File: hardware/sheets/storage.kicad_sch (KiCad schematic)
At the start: 32 parts, among them J1 Conn_02x20_Odd_Even, J2 Conn_02x25_Odd_Even, Q1 2N7002, U1 74HCT04, U10 74HCT573, U11 74HCT138, U2 74HCT08, U3 74HCT08, U4 74HCT32, U5 74HCT125, U6 74HCT138, U7 74HCT138, U8 74HCT245, U9 74HCT573

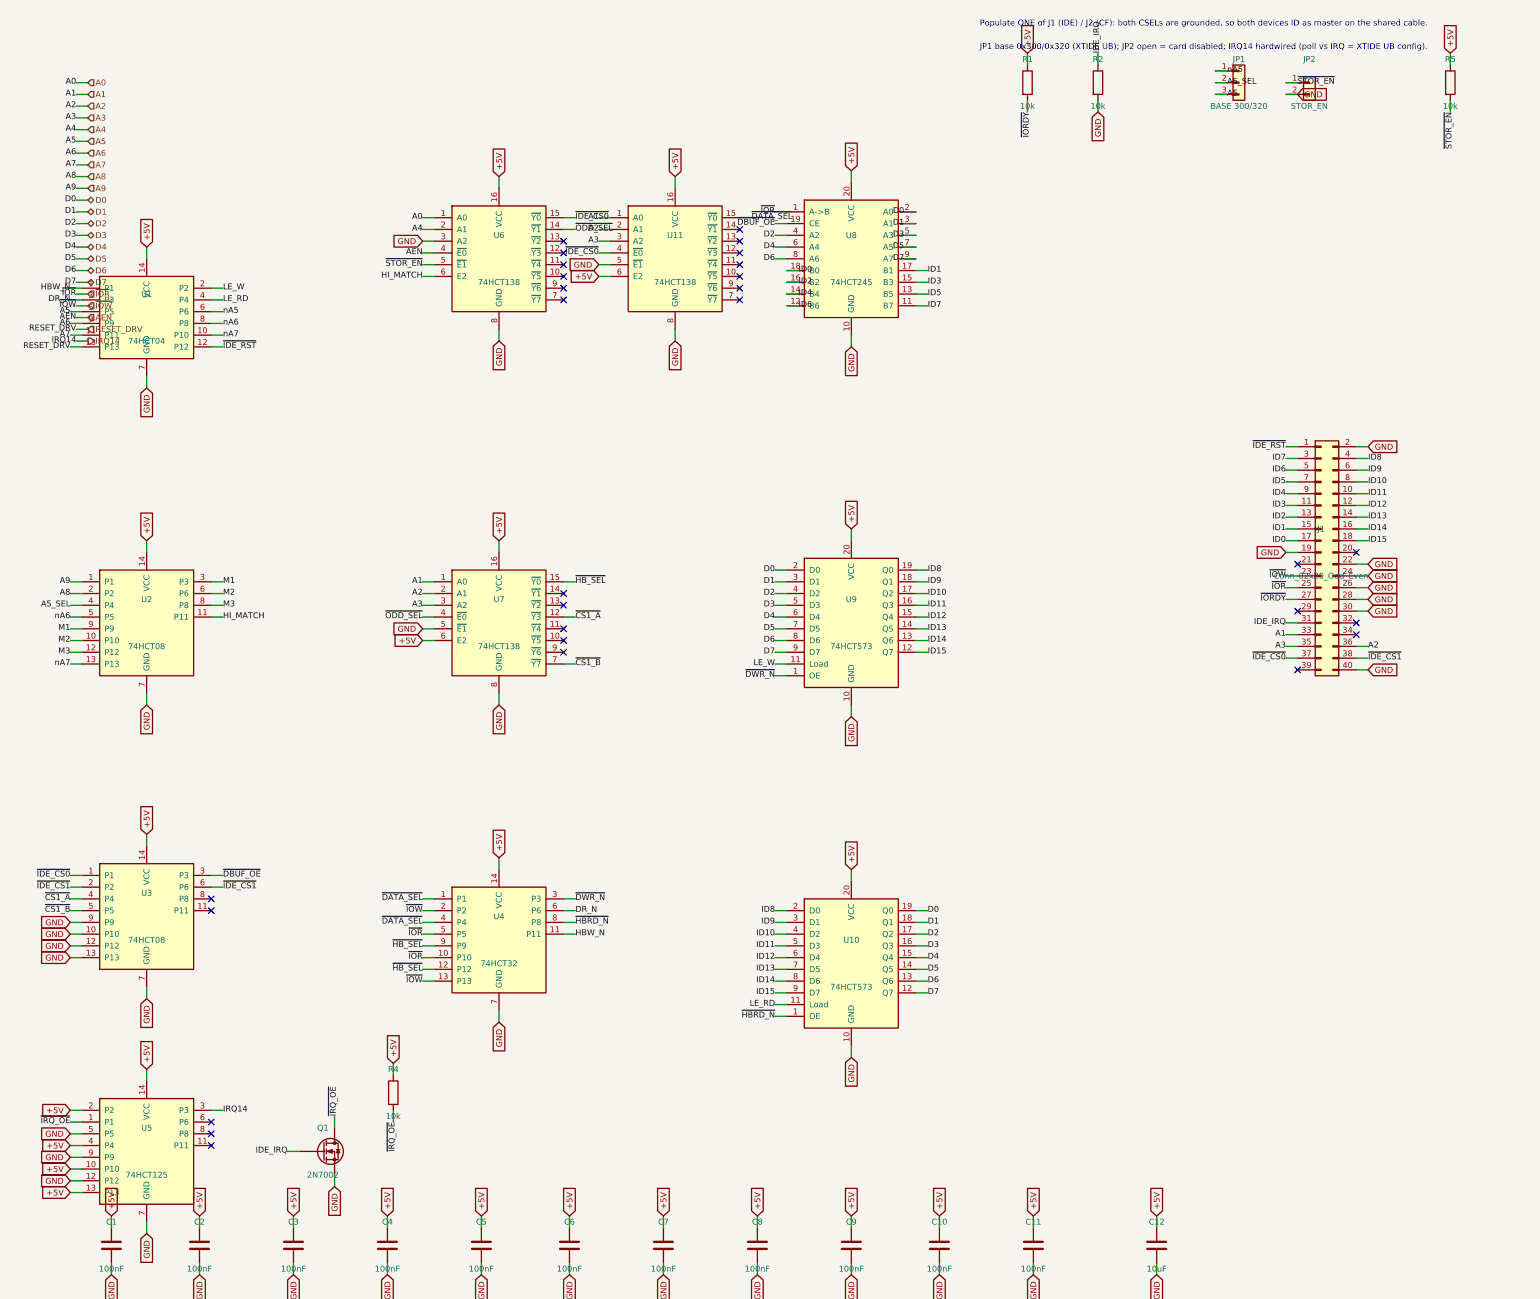
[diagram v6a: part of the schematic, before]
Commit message: com/network/storage/parallel: 3.3V; TL16C550CPT soldered; LVC at external connectors
com_port: PLCC-44 16550 socket -> soldered TL16C550PT (LQFP-48) at +3V3,
rewired signal-for-signal from pins.py (RD/WR split renamed RD1/RD2/WR1/WR2,
INTR->INTRPT, GND->VSS, 8 new NC pins). Decode glue -> HC-grade, IRQ buffer
-> LVC125A, all +3V3. MAX3241 untouched (+5V, spec: already 3.3V-compatible).

network: only U3 (IRQ/AEN gate) moves, to LVC125A @ +3V3 -- RTL8019AS and
its EEPROM stay +5V (datasheet-verified 5V-only part, same treatment as
MAX3241), deviating from a literal reading of the brief's "power sweep"
instruction in favor of its own MAX3241 precedent.

storage: full brief table applied, all +3V3 except the CompactFlash
socket's own VCC power-feed pins (real CF-spec requirement, not a logic
signal).

parallel: brief's swap table only named 8 of 13 chips; traced the DB25
connector's actual net fan-out to fill the gap (U5, U9 also need
5V-tolerant inputs; U6/U7/U8/U12 are purely internal decode -> HC-grade).
U9 reuses the already-bound 74AHC14 value (no bare LVC04A entry exists).

Decisions logged in hardware/notes/questions-{com_port,network,storage,parallel}.md.

Co-Authored-By: Claude Fable 5 <noreply@anthropic.com>
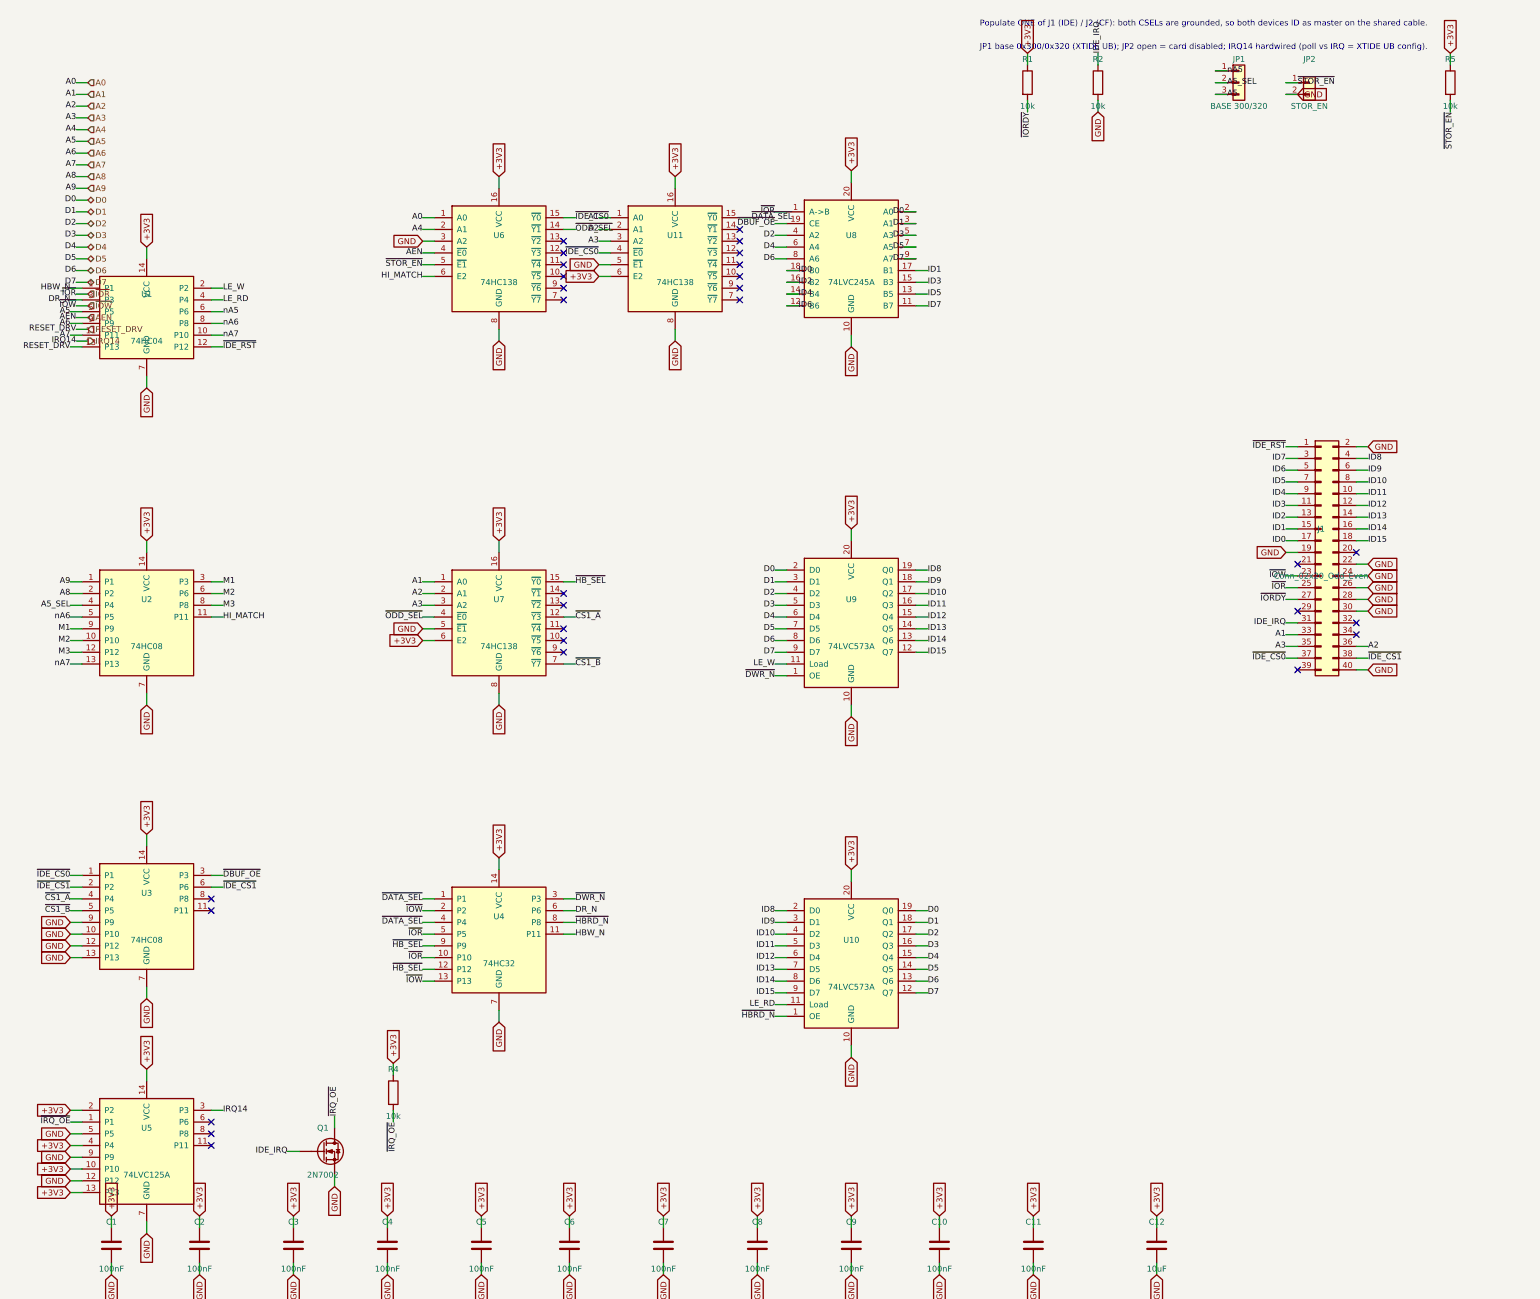
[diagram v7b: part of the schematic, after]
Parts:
- U1: value 74HCT04 -> 74HC04; LCSC Part Num C672096 -> C86613
- U10, U9: value 74HCT573 -> 74LVC573A; footprint Package_SO:SOIC-20W_7.5x12.8mm_P1.27mm -> Package_SO:TSSOP-20_4.4x6.5mm_P0.65mm; LCSC Part Num C5209384 -> C6096
- U11, U6, U7: value 74HCT138 -> 74HC138; LCSC Part Num C5965 -> C5602
- U2, U3: value 74HCT08 -> 74HC08; LCSC Part Num C5959 -> C5593
- U4: value 74HCT32 -> 74HC32; LCSC Part Num C5985 -> C52140395
- U5: value 74HCT125 -> 74LVC125A; LCSC Part Num C5962 -> C6057
- U8: value 74HCT245 -> 74LVC245A; footprint Package_SO:SOIC-20W_7.5x12.8mm_P1.27mm -> Package_SO:TSSOP-20_4.4x6.5mm_P0.65mm; LCSC Part Num C5979 -> C6082
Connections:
- net +5V: no longer C1.1, C10.1, C11.1, C12.1, C2.1, C3.1, C4.1, C5.1, C6.1, C7.1, C8.1, C9.1, R1.1, R4.1, R5.1, U1.14 (VCC), U10.20 (VCC), U11.16 (VCC), U11.6 (E2), U2.14 (VCC), U3.14 (VCC), U4.14 (VCC), U5.10 (P10), U5.13 (P13), U5.14 (VCC), U5.2 (P2), U5.4 (P4), U6.16 (VCC), U7.16 (VCC), U7.6 (E2), U8.20 (VCC), U9.20 (VCC)
- new net +3V3: C1.1, C10.1, C11.1, C12.1, C2.1, C3.1, C4.1, C5.1, C6.1, C7.1, C8.1, C9.1, R1.1, R4.1, R5.1, U1.14 (VCC), U10.20 (VCC), U11.16 (VCC), U11.6 (E2), U2.14 (VCC), U3.14 (VCC), U4.14 (VCC), U5.10 (P10), U5.13 (P13), U5.14 (VCC), U5.2 (P2), U5.4 (P4), U6.16 (VCC), U7.16 (VCC), U7.6 (E2), U8.20 (VCC), U9.20 (VCC)
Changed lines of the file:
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@@
 		)
 	)
-	(global_label "+5V"
+	(global_label "+3V3"
 		(shape input)
 		(at 38.1 60.96 90)
@@
 		)
 	)
-	(global_label "+5V"
+	(global_label "+3V3"
 		(shape input)
 		(at 38.1 124.46 90)
@@
 		)
 	)
-	(global_label "+5V"
+	(global_label "+3V3"
 		(shape input)
 		(at 38.1 187.96 90)
@@
 		)
 	)
-	(global_label "+5V"
+	(global_label "+3V3"
 		(shape input)
 		(at 114.3 193.04 90)
@@
 		)
 	)
-	(global_label "+5V"
+	(global_label "+3V3"
 		(shape input)
 		(at 38.1 238.76 90)
@@
 		)
 	)
-	(global_label "+5V"
+	(global_label "+3V3"
 		(shape input)
 		(at 21.59 247.65 180)
@@
 		)
 	)
-	(global_label "+5V"
+	(global_label "+3V3"
 		(shape input)
 		(at 21.59 255.27 180)
@@
 		)
 	)
-	(global_label "+5V"
+	(global_label "+3V3"
 		(shape input)
 		(at 21.59 260.35 180)
@@
 		)
 	)
-	(global_label "+5V"
+	(global_label "+3V3"
 		(shape input)
 		(at 21.59 265.43 180)
@@
 		)
 	)
-	(global_label "+5V"
+	(global_label "+3V3"
 		(shape input)
 		(at 114.3 45.72 90)
@@
 		)
 	)
-	(global_label "+5V"
+	(global_label "+3V3"
 		(shape input)
 		(at 114.3 124.46 90)
@@
 		)
 	)
-	(global_label "+5V"
+	(global_label "+3V3"
 		(shape input)
 		(at 97.79 146.05 180)
@@
 		)
 	)
-	(global_label "+5V"
+	(global_label "+3V3"
 		(shape input)
 		(at 152.4 45.72 90)
@@
 		)
 	)
-	(global_label "+5V"
+	(global_label "+3V3"
 		(shape input)
 		(at 135.89 67.31 180)
@@
 		)
 	)
-	(global_label "+5V"
+	(global_label "+3V3"
 		(shape input)
 		(at 190.5 44.45 90)
@@
 		)
 	)
-	(global_label "+5V"
+	(global_label "+3V3"
 		(shape input)
 		(at 190.5 121.92 90)
@@
 		)
 	)
-	(global_label "+5V"
+	(global_label "+3V3"
 		(shape input)
 		(at 190.5 195.58 90)
@@
 		)
 	)
-	(global_label "+5V"
+	(global_label "+3V3"
 		(shape input)
 		(at 228.6 19.05 90)
@@
 		)
 	)
-	(global_label "+5V"
+	(global_label "+3V3"
 		(shape input)
 		(at 91.44 237.49 90)
@@
 		)
 	)
-	(global_label "+5V"
+	(global_label "+3V3"
 		(shape input)
 		(at 320.04 19.05 90)
@@
 		)
 	)
-	(global_label "+5V"
+	(global_label "+3V3"
 		(shape input)
 		(at 30.48 270.51 90)
@@
 		)
 	)
-	(global_label "+5V"
+	(global_label "+3V3"
 		(shape input)
 		(at 49.53 270.51 90)
@@
 		)
 	)
-	(global_label "+5V"
+	(global_label "+3V3"
 		(shape input)
 		(at 69.85 270.51 90)
@@
 		)
 	)
-	(global_label "+5V"
+	(global_label "+3V3"
 		(shape input)
 		(at 90.17 270.51 90)
@@
 		)
 	)
-	(global_label "+5V"
+	(global_label "+3V3"
 		(shape input)
 		(at 110.49 270.51 90)
@@
 		)
 	)
-	(global_label "+5V"
+	(global_label "+3V3"
 		(shape input)
 		(at 129.54 270.51 90)
@@
 		)
 	)
-	(global_label "+5V"
+	(global_label "+3V3"
 		(shape input)
 		(at 149.86 270.51 90)
@@
 		)
 	)
-	(global_label "+5V"
+	(global_label "+3V3"
 		(shape input)
 		(at 170.18 270.51 90)
@@
 		)
 	)
-	(global_label "+5V"
+	(global_label "+3V3"
 		(shape input)
 		(at 190.5 270.51 90)
@@
 		)
 	)
-	(global_label "+5V"
+	(global_label "+3V3"
 		(shape input)
 		(at 209.55 270.51 90)
@@
 		)
 	)
-	(global_label "+5V"
+	(global_label "+3V3"
 		(shape input)
 		(at 229.87 270.51 90)
@@
 		)
 	)
-	(global_label "+5V"
+	(global_label "+3V3"
 		(shape input)
 		(at 256.54 270.51 90)
@@
 			)
 		)
-		(property "Value" "74HCT04"
+		(property "Value" "74HC04"
 			(at 38.1 81.28 0)
 			(effects
@@
 			)
 		)
-		(property "LCSC Part Num" "C672096"
+		(property "LCSC Part Num" "C86613"
 			(at 38.1 76.2 0)
 			(effects
@@
 			)
 		)
-		(property "Value" "74HCT08"
+		(property "Value" "74HC08"
 			(at 38.1 147.32 0)
 			(effects
@@
 			)
 		)
-		(property "LCSC Part Num" "C5959"
+		(property "LCSC Part Num" "C5593"
 			(at 38.1 142.24 0)
 			(effects
@@
 			)
 		)
-		(property "Value" "74HCT08"
+		(property "Value" "74HC08"
 			(at 38.1 210.82 0)
 			(effects
@@
 			)
 		)
-		(property "LCSC Part Num" "C5959"
+		(property "LCSC Part Num" "C5593"
 			(at 38.1 205.74 0)
 			(effects
@@
 			)
 		)
-		(property "Value" "74HCT32"
+		(property "Value" "74HC32"
 			(at 114.3 215.9 0)
 			(effects
@@
 			)
 		)
-		(property "LCSC Part Num" "C5985"
+		(property "LCSC Part Num" "C52140395"
 			(at 114.3 210.82 0)
 			(effects
@@
 			)
 		)
-		(property "Value" "74HCT125"
+		(property "Value" "74LVC125A"
 			(at 38.1 261.62 0)
 			(effects
@@
 			)
 		)
-		(property "LCSC Part Num" "C5962"
+		(property "LCSC Part Num" "C6057"
 			(at 38.1 256.54 0)
 			(effects
@@
 			)
 		)
-		(property "Value" "74HCT138"
+		(property "Value" "74HC138"
 			(at 114.3 68.58 0)
 			(effects
@@
 			)
 		)
-		(property "LCSC Part Num" "C5965"
+		(property "LCSC Part Num" "C5602"
 			(at 114.3 63.5 0)
 			(effects
@@
 			)
 		)
-		(property "Value" "74HCT138"
+		(property "Value" "74HC138"
 			(at 114.3 147.32 0)
 			(effects
@@
 			)
 		)
-		(property "LCSC Part Num" "C5965"
+		(property "LCSC Part Num" "C5602"
 			(at 114.3 142.24 0)
 			(effects
@@
 			)
 		)
-		(property "Value" "74HCT138"
+		(property "Value" "74HC138"
 			(at 152.4 68.58 0)
 			(effects
@@
 			)
 		)
-		(property "LCSC Part Num" "C5965"
+		(property "LCSC Part Num" "C5602"
 			(at 152.4 63.5 0)
 			(effects
@@
 			)
 		)
-		(property "Value" "74HCT245"
+		(property "Value" "74LVC245A"
 			(at 190.5 68.58 0)
 			(effects
@@
 			)
 		)
-		(property "Footprint" "Package_SO:SOIC-20W_7.5x12.8mm_P1.27mm"
+		(property "Footprint" "Package_SO:TSSOP-20_4.4x6.5mm_P0.65mm"
 			(at 190.5 63.5 0)
 			(effects
@@
 			)
 		)
-		(property "LCSC Part Num" "C5979"
+		(property "LCSC Part Num" "C6082"
 			(at 190.5 63.5 0)
 			(effects
@@
 			)
 		)
-		(property "Value" "74HCT573"
+		(property "Value" "74LVC573A"
 			(at 190.5 147.32 0)
 			(effects
@@
 			)
 		)
-		(property "Footprint" "Package_SO:SOIC-20W_7.5x12.8mm_P1.27mm"
+		(property "Footprint" "Package_SO:TSSOP-20_4.4x6.5mm_P0.65mm"
 			(at 190.5 142.24 0)
 			(effects
@@
 			)
 		)
-		(property "LCSC Part Num" "C5209384"
+		(property "LCSC Part Num" "C6096"
 			(at 190.5 142.24 0)
 			(effects
@@
 			)
 		)
-		(property "Value" "74HCT573"
+		(property "Value" "74LVC573A"
 			(at 190.5 220.98 0)
 			(effects
@@
 			)
 		)
-		(property "Footprint" "Package_SO:SOIC-20W_7.5x12.8mm_P1.27mm"
+		(property "Footprint" "Package_SO:TSSOP-20_4.4x6.5mm_P0.65mm"
 			(at 190.5 215.9 0)
 			(effects
@@
 			)
 		)
-		(property "LCSC Part Num" "C5209384"
+		(property "LCSC Part Num" "C6096"
 			(at 190.5 215.9 0)
 			(effects
